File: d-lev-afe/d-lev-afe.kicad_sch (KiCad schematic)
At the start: 36 parts, among them J1 S8B-PH-SM4-TB, Q1 MMBT3904, Q2 MMBT3906, U1 74AHC04, U2 AP2112K-3.3, U3 SRV05-4

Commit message: Add iBOMs and additional part numbers
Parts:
- AE1, AE2: MPN (none) -> 5331; Supplier (none) -> Mouser; Supplier URL (none) -> https://www.mouser.com/ProductDetail/Keystone-Electronics/5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
- C1, C7: value 0.1uF -> 100n; MPN (none) -> GRM188R71E104KA01D; Notes (none) -> Common; Supplier (none) -> Digi-Key; Supplier URL (none) -> https://www.digikey.com/en/products/detail/murata-electroni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
- C10: value 1p -> 2.4p; DNP (none) -> Y; MPN (none) -> 08052U2R4BAT2A; Notes (none) -> Class 1 200V; Supplier (none) -> Mouser; Supplier URL (none) -> https://www.mouser.com/ProductDetail/581-08052U2R4BAT2A
- C2: value .1u -> 100n; MPN (none) -> GRM188R71E104KA01D; Notes (none) -> Common; Supplier (none) -> Digi-Key; Supplier URL (none) -> https://www.digikey.com/en/products/detail/murata-electroni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
- C4, C6: MPN (none) -> CL21A106KAYNNNG; Supplier (none) -> Mouser; Supplier URL (none) -> https://www.mouser.com/ProductDetail/187-CL21A106KAYNNNG
- C8: MPN (none) -> VJ0805D1R0DXPAJ; Notes (none) -> Class 1 200V; Supplier (none) -> Mouser; Supplier URL (none) -> https://www.mouser.com/ProductDetail/77-VJ0805D1R0DXPAJ
- C9: MPN (none) -> C0603C101K8RACAUTO; Supplier (none) -> Mouser
- H1, H2, H3, H5: MPN (none) -> SMTSO-M3-2ET; Supplier (none) -> Mouser; Supplier Alt (none) -> Aliexpress; Supplier Alt URL (none) -> https://www.aliexpress.us/item/3256803593796853.html; Supplier URL (none) -> https://www.mouser.com/ProductDetail/PEM/SMTSO-M3-2ET?qs=l4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
- H4: MPN (none) -> SMTSO-M4-8ET; Supplier (none) -> Mouser; Supplier Alt (none) -> Aliexpress; Supplier Alt URL (none) -> https://www.aliexpress.us/item/3256805247930963.html?spm=a2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; Supplier URL (none) -> https://www.mouser.com/ProductDetail/PEM/SMTSO-M4-8ET?qs=l4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
- J1: MPN (none) -> S8B-PH-SM4-TB; Supplier (none) -> Digi-Key; Supplier Alt (none) -> Aliexpress; Supplier Alt URL (none) -> https://www.aliexpress.us/item/3256805227213161.html; Supplier URL (none) -> https://www.digikey.com/en/products/detail/jst-sales-americ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
- L1: MPN (none) -> 2ZFF4-252k-DM; Notes (none) -> BTO, request either 1mH or 2mH; Supplier (none) -> Alibaba; Supplier URL (none) -> https://www.alibaba.com/product-detail/2-5mH-CHOKE_16006311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; Tolerance (none) -> 10%
- L2, L3: DNP (none) -> Y; MPN (none) -> DO1605T-105MLC; Notes (none) -> DNP if L1 populated; Supplier (none) -> Mouser; Supplier Alt (none) -> Coilcraft; Supplier Alt URL (none) -> https://www.coilcraft.com/en-us/products/power/unshielded-i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; Supplier URL (none) -> https://www.mouser.com/ProductDetail/Coilcraft/DO1605T-105M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; Tolerance (none) -> 20%
- Q1: MPN (none) -> MMBT3904-7-F; Supplier (none) -> Mouser; Supplier URL (none) -> https://www.mouser.com/ProductDetail/Diodes-Incorporated/MM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
- Q2: MPN (none) -> MMBT3906-7-F; Supplier (none) -> Mouser; Supplier URL (none) -> https://www.mouser.com/ProductDetail/Diodes-Incorporated/MM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
- R10, R2, R9: DNP (none) -> Y
- R6: value 220K -> 220k; MPN (none) -> RC0603FR-13220KL; Supplier (none) -> Mouser
- U1: MPN (none) -> SN74AHC04DRG4; Supplier (none) -> Mouser; Supplier URL (none) -> https://www.mouser.com/ProductDetail/Texas-Instruments/SN74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
- U2: MPN (none) -> AP2112K-3.3TRG1; Supplier (none) -> Mouser; Supplier URL (none) -> https://www.mouser.com/ProductDetail/Diodes-Incorporated/AP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
- U3: MPN (none) -> SRV05-4L-TP; Supplier (none) -> Mouser; Supplier URL (none) -> https://www.mouser.com/ProductDetail/Micro-Commercial-Compo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

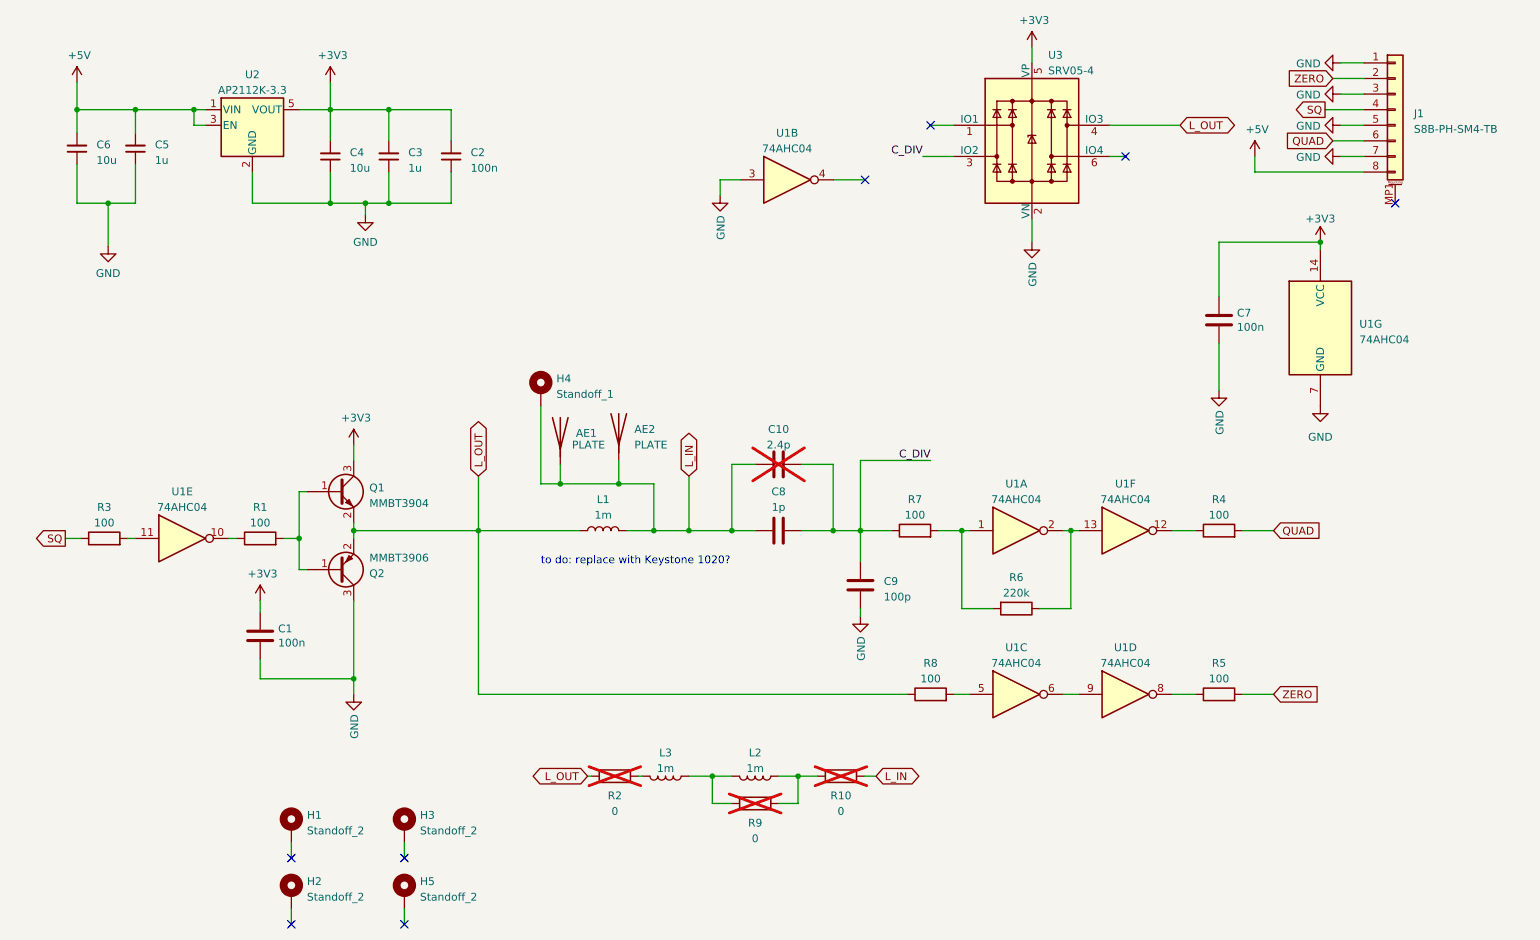
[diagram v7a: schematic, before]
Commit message: d-lev-afe: switch to 2 layers, add 'antenna' version, pick out JLC parts
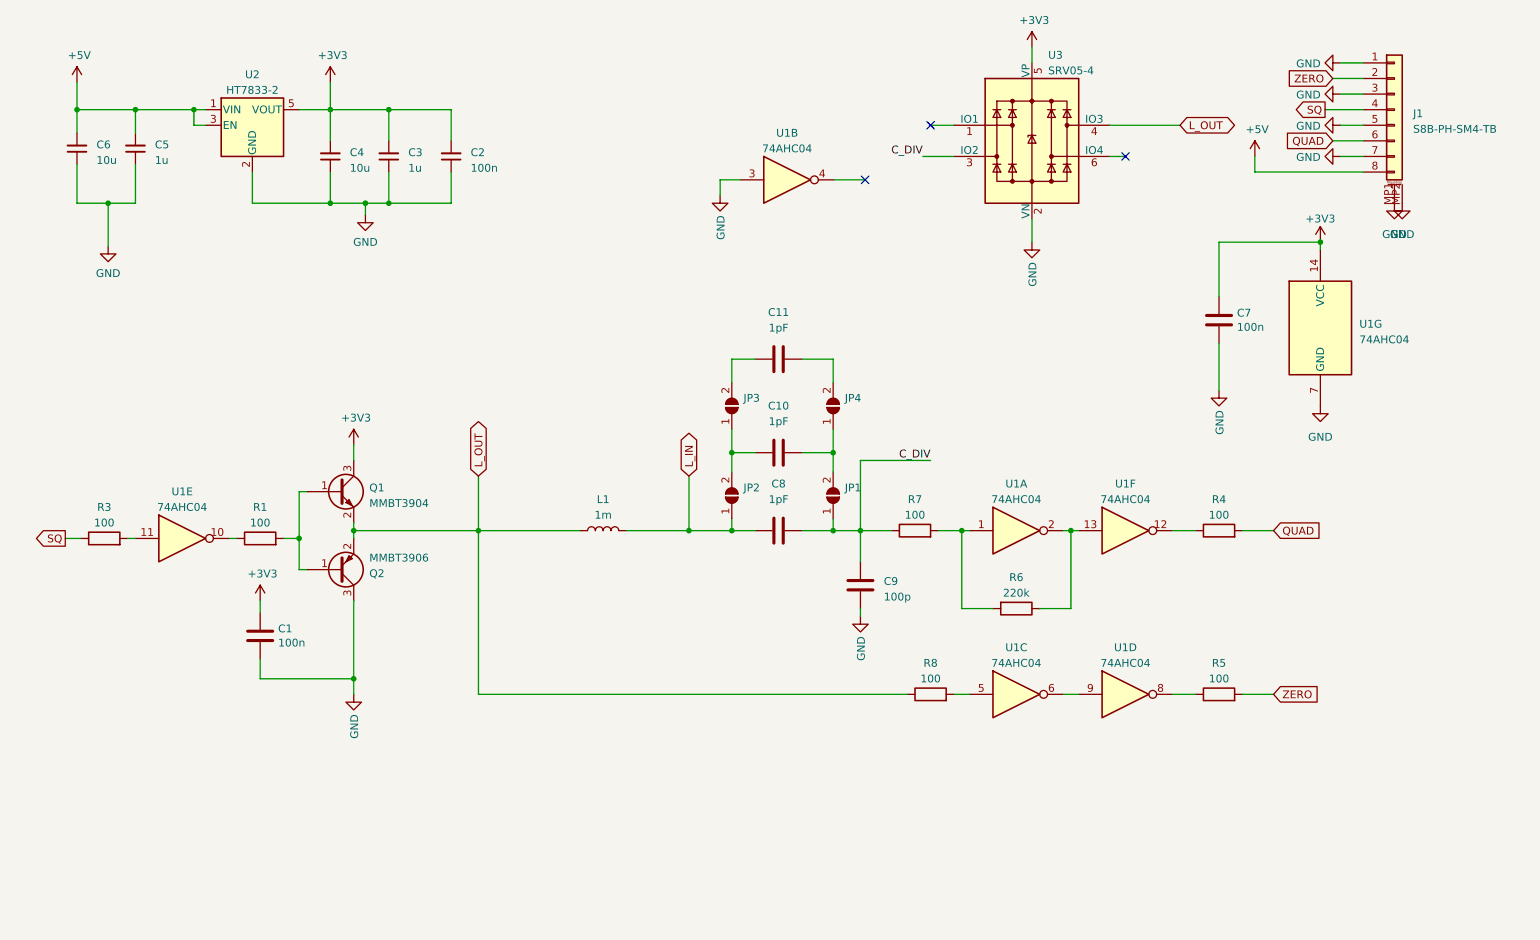
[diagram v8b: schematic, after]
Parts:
- removed AE1, AE2: PLATE, theremin:keystone-PN5331TR, symbol Device:Antenna
- removed H1, H2, H3, H5: Standoff_2, theremin:SMTSO-M3, symbol Mechanical:MountingHole_Pad
- removed H4: Standoff_1, theremin:SMTSO-M4, symbol Mechanical:MountingHole_Pad
- removed L2, L3: 1m, theremin:Coilcraft_DO1605T, symbol Device:L
- removed R10, R2, R9: 0, Resistor_SMD:R_0603_1608Metric, symbol Device:R
- added C11: 1pF, theremin:testpoint_cap_1pf, symbol Device:C
- added JP1, JP2, JP3, JP4: SolderJumper_2_Open, theremin:SolderJumper-0.5mm-Tiny, symbol Jumper:SolderJumper_2_Open
- C1, C2, C7: LCSC (none) -> C14663
- C10: value 2.4p -> 1pF; footprint Capacitor_SMD:C_0805_2012Metric_Pad1.18x1.45mm_HandSolder -> theremin:testpoint_cap_1pf; DNP Y -> (none); MPN 08052U2R4BAT2A -> (none); Notes Class 1 200V -> (none); Supplier Mouser -> (none); Supplier URL https://www.mouser.com/ProductDetail/581-08052U2R4BAT2A -> (none); now fitted; now left out of the parts list
- C3, C5: LCSC (none) -> C15849
- C4, C6: LCSC (none) -> C440198
- C8: value 1p -> 1pF; footprint Capacitor_SMD:C_0805_2012Metric_Pad1.18x1.45mm_HandSolder -> theremin:testpoint_cap_1pf; MPN VJ0805D1R0DXPAJ -> (none); Notes Class 1 200V -> (none); Supplier Mouser -> (none); Supplier URL https://www.mouser.com/ProductDetail/77-VJ0805D1R0DXPAJ -> (none); now left out of the parts list
- C9: LCSC (none) -> C14858
- J1: LCSC (none) -> C265121
- Q1: LCSC (none) -> C20526
- Q2: LCSC (none) -> C2143
- R1, R3, R4, R5, R7, R8: LCSC (none) -> C22775
- R6: LCSC (none) -> C22961
- U1: LCSC (none) -> C8131
- U2: value AP2112K-3.3 -> HT7833-2; LCSC (none) -> C164106; MPN AP2112K-3.3TRG1 -> HT7833-2; Supplier Mouser -> (none); Supplier URL https://www.mouser.com/ProductDetail/Diodes-Incorporated/AP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 -> (none)
- U3: LCSC (none) -> C85364
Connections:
- net C_DIV: now also C8.1, JP1.1 (A); no longer C10.2, C8.2
- net GND: now also J1.MP1 (MountPin1), J1.MP2 (MountPin2)
- net L_IN: now also C8.2, JP2.1 (A); no longer C10.1, C8.1
- new net: C10.2, JP2.2 (B), JP3.1 (A)
- new net: C11.1, JP4.2 (B)
- new net: C11.2, JP3.2 (B)
- new net: C10.1, JP1.2 (B), JP4.1 (A)
- no-connect marks 8 -> 3
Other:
- note removed: "to do: replace with Keystone 1020?"
- moved on the sheet: C8
